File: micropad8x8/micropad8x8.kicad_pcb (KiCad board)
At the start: 2 copper layers, 257.2 x 88.6 mm, 41 parts, among them U1 Raspberry_Pi_Pico

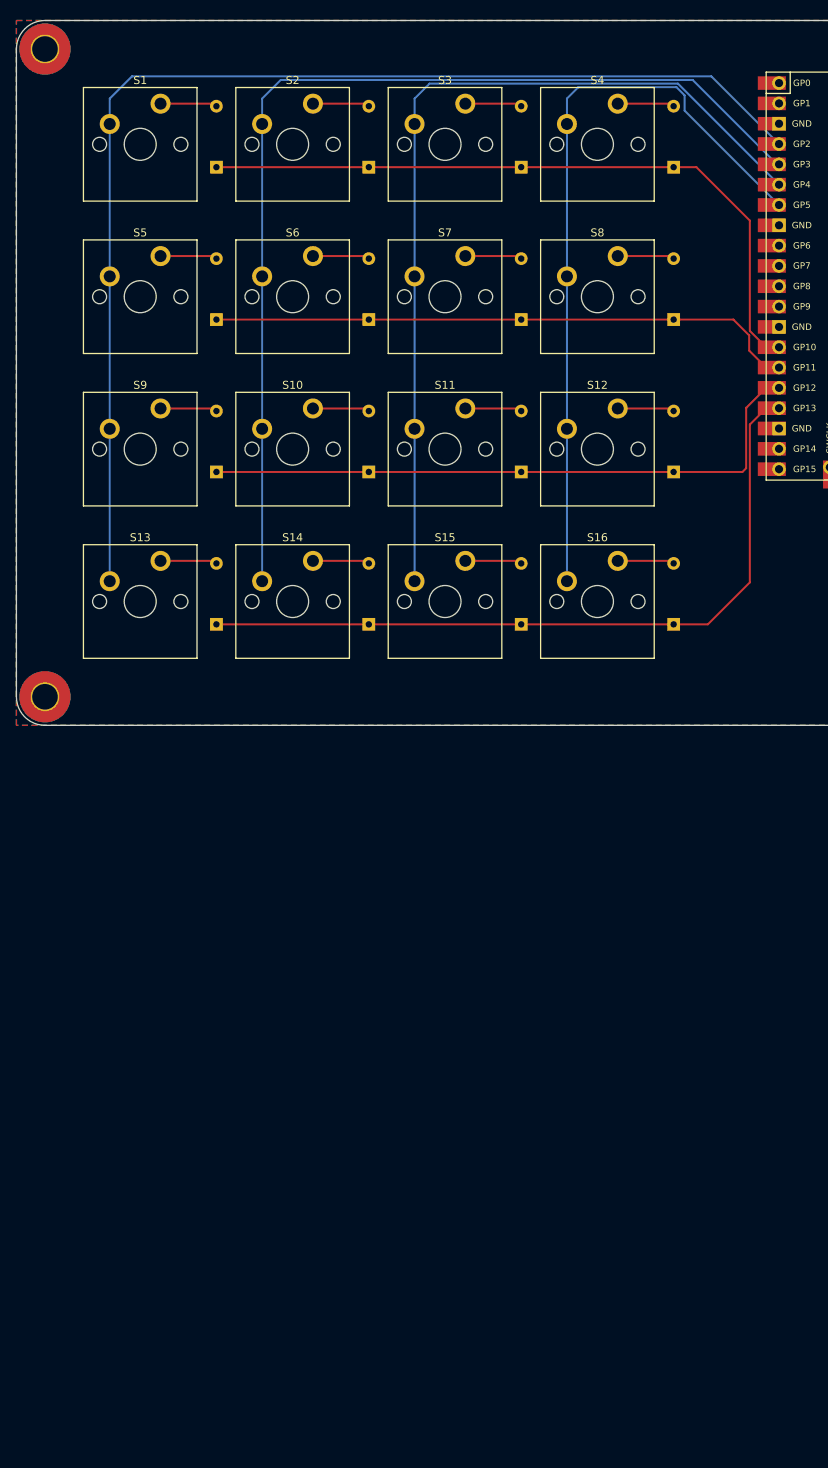
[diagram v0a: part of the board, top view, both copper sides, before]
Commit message: added top layer
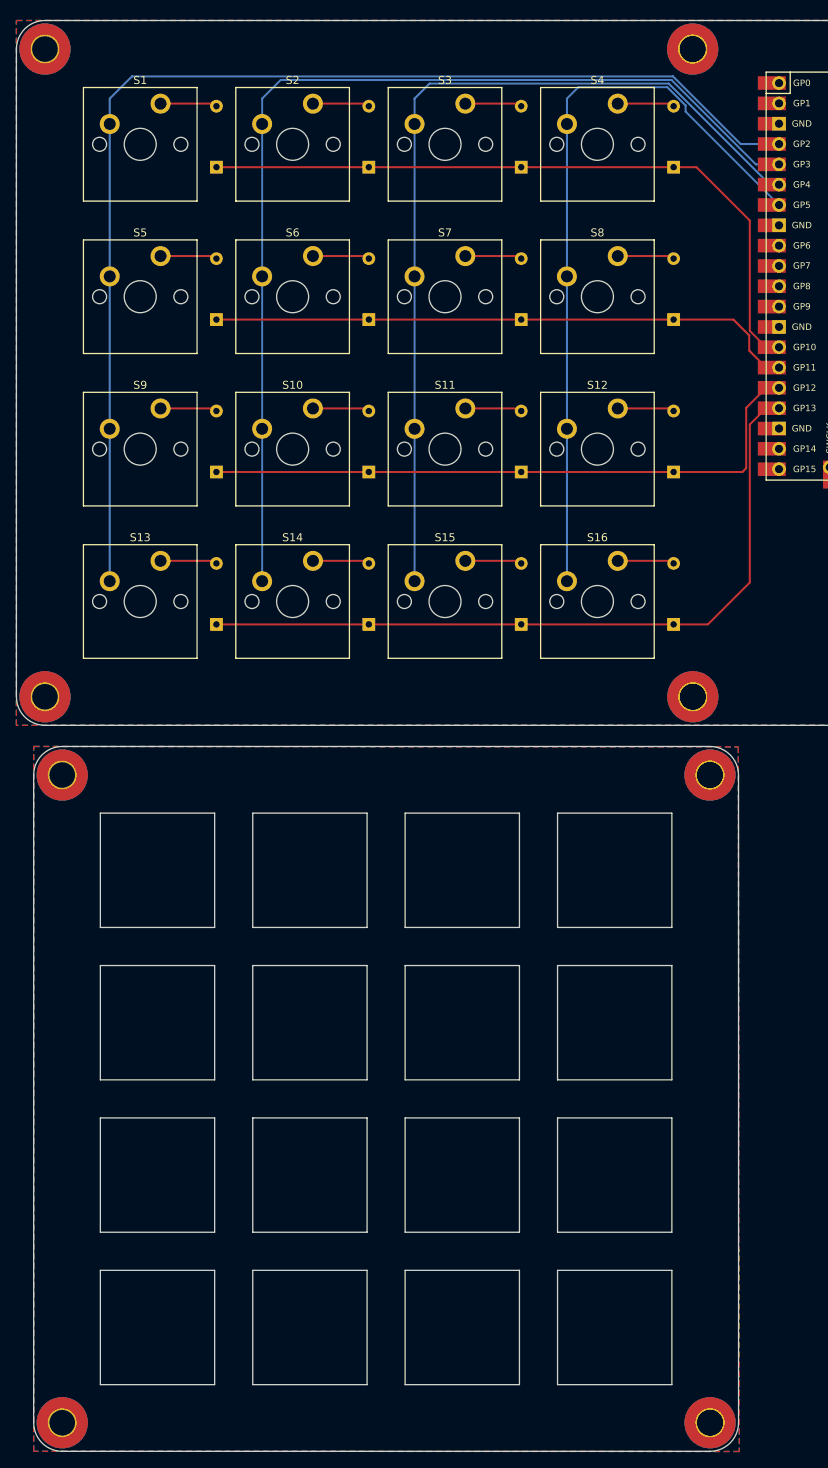
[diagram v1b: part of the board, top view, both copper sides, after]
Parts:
- added ?: , , F.Cu at (107.3, 20.6)
- added ?: , , F.Cu at (109.5, 192.3)
- added ?: , , F.Cu at (109.5, 111.4)
- added ?: , , F.Cu at (107.3, 101.6)
- added REF**: MountingHole_3.2mm_M3_Pad_TopBottom, MountingHole:MountingHole_3.2mm_M3_Pad_TopBottom, F.Cu at (107.3, 20.6)
- added REF**: MountingHole_3.2mm_M3_Pad_TopBottom, MountingHole:MountingHole_3.2mm_M3_Pad_TopBottom, F.Cu at (109.5, 111.4)
- added REF**: MountingHole_3.2mm_M3_Pad_TopBottom, MountingHole:MountingHole_3.2mm_M3_Pad_TopBottom, F.Cu at (107.3, 101.6)
- added REF**: MountingHole_3.2mm_M3_Pad_TopBottom, MountingHole:MountingHole_3.2mm_M3_Pad_TopBottom, F.Cu at (28.5, 192.3)
- added REF**: MountingHole_3.2mm_M3_Pad_TopBottom, MountingHole:MountingHole_3.2mm_M3_Pad_TopBottom, F.Cu at (109.5, 192.3)
- added REF**: MountingHole_3.2mm_M3_Pad_TopBottom, MountingHole:MountingHole_3.2mm_M3_Pad_TopBottom, F.Cu at (28.5, 111.4)
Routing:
- net Col 3: track 94.6 -> 94.0 mm
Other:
- board size 257.2 x 88.6 mm -> 257.2 x 179.4 mm

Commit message: minor changes
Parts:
- added ?: , , F.Cu at (191.8, 188.6)
- added ?: , , F.Cu at (191.8, 107.6)
- added REF**: MountingHole_3.2mm_M3_Pad_TopBottom, MountingHole:MountingHole_3.2mm_M3_Pad_TopBottom, F.Cu at (110.8, 188.6)
- added REF**: MountingHole_3.2mm_M3_Pad_TopBottom, MountingHole:MountingHole_3.2mm_M3_Pad_TopBottom, F.Cu at (110.8, 107.6)
- added REF**: MountingHole_3.2mm_M3_Pad_TopBottom, MountingHole:MountingHole_3.2mm_M3_Pad_TopBottom, F.Cu at (191.8, 188.6)
- added REF**: MountingHole_3.2mm_M3_Pad_TopBottom, MountingHole:MountingHole_3.2mm_M3_Pad_TopBottom, F.Cu at (191.8, 107.6)
- moved REF** 16.7 mm to (259.7, 99.5)
- moved REF** 16.7 mm to (145.4, 18.5)
- moved REF** 16.7 mm to (145.4, 99.5)
- moved REF** 16.7 mm to (259.7, 18.5)
- moved REF** 9.05 mm to (20.2, 107.8)
- moved ? 9.05 mm to (101.2, 107.8)
- moved REF** 9.05 mm to (101.2, 107.8)
- moved REF** 9.05 mm to (20.2, 188.8)
- moved ? 9.05 mm to (101.2, 188.8)
- moved REF** 9.05 mm to (101.2, 188.8)
- moved D9 7.46 mm to (40.7, 71.1)
- moved D1 7.46 mm to (40.7, 33.0)
- moved D5 7.46 mm to (40.7, 52.0)
- moved S7 7.46 mm to (69.3, 49.2)
- moved S8 7.46 mm to (88.4, 49.2)
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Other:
- board size 257.2 x 179.4 mm -> 247.6 x 177.7 mm
